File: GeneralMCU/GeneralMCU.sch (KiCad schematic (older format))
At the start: 98 parts, among them J1 ARM_JTAG_SWD, J2 SMD castellation PKG, J3 USB_B_Micro, J4 Conn_01x04, J5 PWR, J6 OLED, Q1 Q_NMOS_DGS, SW1 USER, SW2 RESET, U1 STM32F303R6Tx, U2 SN65HVD230, U3 AZ1117-3.3, U4 P78E05-1000, U5 DS18B20, Y1 32.768kHz, Y2 8MHz

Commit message: Can't remember these changes lol
From the meeting, switching back to branch now.
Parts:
- added snblock1, snblock2: Logo_Open_Hardware_Small, µ104KiCAD:SN_BLOCK, symbol Graphic:Logo_Open_Hardware_Small
- added snblock3, snblock4, snblock8: Logo_Open_Hardware_Small, µ104KiCAD:Paradigm_Logo_Very_Small, symbol Graphic:Logo_Open_Hardware_Small
- added snblock5: Logo_Open_Hardware_Small, Symbol:KiCad-Logo2_8mm_SilkScreen, symbol Graphic:Logo_Open_Hardware_Small
- added snblock6, snblock7: Logo_Open_Hardware_Small, Symbol:ESD-Logo_6.6x6mm_SilkScreen, symbol Graphic:Logo_Open_Hardware_Small
- F1: value 32VDC 1A PTC -> 3VDC 1A PTC
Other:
- note added: "*Vin = 9 - 30V\n\n"
- note removed: "*Vin = 9 - 32V\n\n"
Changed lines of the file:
@@
 $EndComp
 Text Notes 480  3290 0    39   ~ 0
-*Vin = 9 - 32V\n\n
+*Vin = 9 - 30V\n\n
 Wire Wire Line
 	1530 2970 1530 2890
@@
 P 1770 2970
 F 0 "F1" H 1690 3040 50  0000 C CNN
-F 1 "32VDC 1A PTC" H 1780 2910 28  0000 C CNN
+F 1 "3VDC 1A PTC" H 1780 2910 28  0000 C CNN
 F 2 "Diodes_SMD:D_1206" H 1770 2970 50  0001 C CNN
 F 3 "~" H 1770 2970 50  0001 C CNN
@@
 	1    0    0    -1
 $EndComp
+$Comp
+L Graphic:Logo_Open_Hardware_Small snblock1
+U 1 1 5DAB9BAE
+P 11960 7730
+F 0 "snblock1" H 11960 8005 50  0001 C CNN
+F 1 "Logo_Open_Hardware_Small" H 11960 7505 50  0001 C CNN
+F 2 "µ104KiCAD:SN_BLOCK" H 11960 7730 50  0001 C CNN
+F 3 "~" H 11960 7730 50  0001 C CNN
+	1    11960 7730
+	1    0    0    -1
+$EndComp
+$Comp
+L Graphic:Logo_Open_Hardware_Small snblock2
+U 1 1 5DABADF3
+P 11970 7300
+F 0 "snblock2" H 11970 7575 50  0001 C CNN
+F 1 "Logo_Open_Hardware_Small" H 11970 7075 50  0001 C CNN
+F 2 "µ104KiCAD:SN_BLOCK" H 11970 7300 50  0001 C CNN
+F 3 "~" H 11970 7300 50  0001 C CNN
+	1    11970 7300
+	1    0    0    -1
+$EndComp
+$Comp
+L Graphic:Logo_Open_Hardware_Small snblock3
+U 1 1 5DAEEBEF
+P 11960 6850
+F 0 "snblock3" H 11960 7125 50  0001 C CNN
+F 1 "Logo_Open_Hardware_Small" H 11960 6625 50  0001 C CNN
+F 2 "µ104KiCAD:Paradigm_Logo_Very_Small" H 11960 6850 50  0001 C CNN
+F 3 "~" H 11960 6850 50  0001 C CNN
+	1    11960 6850
+	1    0    0    -1
+$EndComp
+$Comp
+L Graphic:Logo_Open_Hardware_Small snblock4
+U 1 1 5DAF1C52
+P 11970 6400
+F 0 "snblock4" H 11970 6675 50  0001 C CNN
+F 1 "Logo_Open_Hardware_Small" H 11970 6175 50  0001 C CNN
+F 2 "µ104KiCAD:Paradigm_Logo_Very_Small" H 11970 6400 50  0001 C CNN
+F 3 "~" H 11970 6400 50  0001 C CNN
+	1    11970 6400
+	1    0    0    -1
+$EndComp
+$Comp
+L Graphic:Logo_Open_Hardware_Small snblock8
+U 1 1 5DAF1E56
+P 12500 6410
+F 0 "snblock8" H 12500 6685 50  0001 C CNN
+F 1 "Logo_Open_Hardware_Small" H 12500 6185 50  0001 C CNN
+F 2 "µ104KiCAD:Paradigm_Logo_Very_Small" H 12500 6410 50  0001 C CNN
+F 3 "~" H 12500 6410 50  0001 C CNN
+	1    12500 6410
+	1    0    0    -1
+$EndComp
+$Comp
+L Graphic:Logo_Open_Hardware_Small snblock6
+U 1 1 5DAF2182
+P 12480 6880
+F 0 "snblock6" H 12480 7155 50  0001 C CNN
+F 1 "Logo_Open_Hardware_Small" H 12480 6655 50  0001 C CNN
+F 2 "Symbol:ESD-Logo_6.6x6mm_SilkScreen" H 12480 6880 50  0001 C CNN
+F 3 "~" H 12480 6880 50  0001 C CNN
+	1    12480 6880
+	1    0    0    -1
+$EndComp
+$Comp
+L Graphic:Logo_Open_Hardware_Small snblock7
+U 1 1 5DAF2490
+P 12480 7310
+F 0 "snblock7" H 12480 7585 50  0001 C CNN
+F 1 "Logo_Open_Hardware_Small" H 12480 7085 50  0001 C CNN
+F 2 "Symbol:ESD-Logo_6.6x6mm_SilkScreen" H 12480 7310 50  0001 C CNN
+F 3 "~" H 12480 7310 50  0001 C CNN
+	1    12480 7310
+	1    0    0    -1
+$EndComp
+$Comp
+L Graphic:Logo_Open_Hardware_Small snblock5
+U 1 1 5DAF2789
+P 12470 7730
+F 0 "snblock5" H 12470 8005 50  0001 C CNN
+F 1 "Logo_Open_Hardware_Small" H 12470 7505 50  0001 C CNN
+F 2 "Symbol:KiCad-Logo2_8mm_SilkScreen" H 12470 7730 50  0001 C CNN
+F 3 "~" H 12470 7730 50  0001 C CNN
+	1    12470 7730
+	1    0    0    -1
+$EndComp

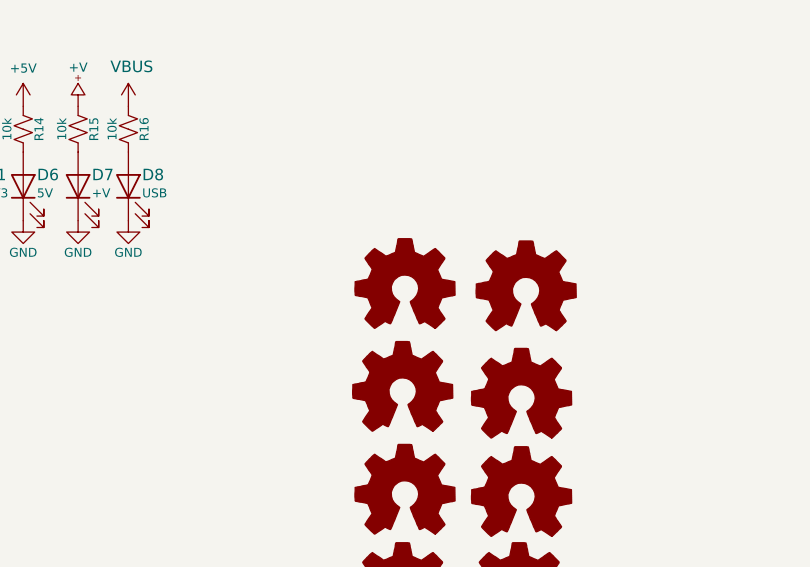
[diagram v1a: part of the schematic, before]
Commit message: Fixed castellated pads. Ready for review
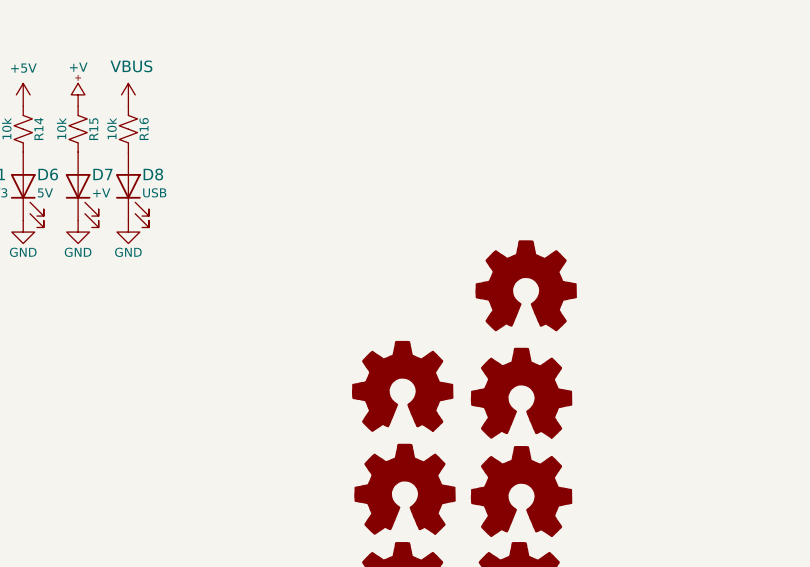
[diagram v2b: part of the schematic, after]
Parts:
- removed snblock4: Logo_Open_Hardware_Small, µ104KiCAD:Paradigm_Logo_Very_Small, symbol Graphic:Logo_Open_Hardware_Small
- snblock5: footprint Symbol:KiCad-Logo2_8mm_SilkScreen -> Symbol:KiCad-Logo_8mm_SilkScreen
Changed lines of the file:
@@
-$EndComp
-$Comp
-L Graphic:Logo_Open_Hardware_Small snblock4
-U 1 1 5DAF1C52
-P 11970 6400
-F 0 "snblock4" H 11970 6675 50  0001 C CNN
-F 1 "Logo_Open_Hardware_Small" H 11970 6175 50  0001 C CNN
-F 2 "µ104KiCAD:Paradigm_Logo_Very_Small" H 11970 6400 50  0001 C CNN
-F 3 "~" H 11970 6400 50  0001 C CNN
-	1    11970 6400
-	1    0    0    -1
 $EndComp
 $Comp
@@
 F 0 "snblock5" H 12470 8005 50  0001 C CNN
 F 1 "Logo_Open_Hardware_Small" H 12470 7505 50  0001 C CNN
-F 2 "Symbol:KiCad-Logo2_8mm_SilkScreen" H 12470 7730 50  0001 C CNN
+F 2 "Symbol:KiCad-Logo_8mm_SilkScreen" H 12470 7730 50  0001 C CNN
 F 3 "~" H 12470 7730 50  0001 C CNN
 	1    12470 7730

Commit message: Added silk and generated gerbers. Review me.
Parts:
- removed J2: SMD castellation PKG, µ104KiCAD:PAD42, symbol GeneralMCU-rescue:Conn_02x21_Counter_Clockwise-Connector_Generic
- added J2: SMD46 castellation PKG, µ104KiCAD:PAD42, symbol GeneralMCU-Example:SMD46
- added snblock10: Logo_Open_Hardware_Small, pics:stride, symbol Graphic:Logo_Open_Hardware_Small
- added snblock11: Logo_Open_Hardware_Small, pics:MUN, symbol Graphic:Logo_Open_Hardware_Small
- added snblock4: Logo_Open_Hardware_Small, pics:poddy, symbol Graphic:Logo_Open_Hardware_Small
- added snblock9: Logo_Open_Hardware_Small, pics:datboi, symbol Graphic:Logo_Open_Hardware_Small
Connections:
- net +3V3: now also J2.3
- net +5V: now also J2.2
- net +V: now also J2.26
- net CANH: now also J2.19
- net CANL: now also J2.18
- net CAN_Shield: now also J2.20
- net CHASSIS: now also J2.21
- net GND: now also J2.1, J2.22, J2.25
- net I2C1_SCL: now also J2.38
- net I2C1_SDA: now also J2.39
- net PA0: now also J2.44
- net PA1: now also J2.45
- net PA10: now also J2.27
- net PA2: now also J2.46
- net PA4: now also J2.4
- net PA5: now also J2.5
- net PA6: now also J2.6
- net PA7: now also J2.7
- net PA8: now also J2.29
- net PA9: now also J2.28
- net PB0: now also J2.10
- net PB1: now also J2.14
- net PB10: now also J2.12
- net PB11: now also J2.11
- net PB12: now also J2.15
- net PB13: now also J2.16
- net PB14: now also J2.17
- net PB15: now also J2.34
- net PB2: now also J2.13
- net PC0: now also J2.40
- net PC1: now also J2.41
- net PC10: now also J2.35
- net PC11: now also J2.36
- net PC12: now also J2.37
- net PC2: now also J2.42
- net PC3: now also J2.43
- net PC4: now also J2.8
- net PC5: now also J2.9
- net PC6: now also J2.33
- net PC7: now also J2.32
- net PC8: now also J2.31
- net PC9: now also J2.30
- no-connect marks 5 -> 7
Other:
- note added: "Drop In PCB Spec:\n1) CAN - Place TVS diode and bus filter caps close to CAN connector\n2) Provide power through J2 SMD pad within range from J5\n\n\n\nAssembly:\n1) Trim and file U4, and J6 THT flat on bottom off PCB\n2) Insert J3 jumper if powering over USB\n3) Solder jumper JP1 and JP2 for CAN terminations\n"
- note added: "GeneralMCU"
- note removed: "Drop In PCB Spec:\n1) CAN - Place TVS diode and bus filter caps close to CAN connector\n\n"
- note removed: "PARADUINO"

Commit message: Updated BOM
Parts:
- removed BZ1: Buzzer, Buzzer_Beeper:Buzzer_Murata_PKMCS0909E4000-R1, symbol GeneralMCU-rescue:Buzzer-Device
- removed C1, C11, C13, C15, C18, C19, C36, C6, C7, C9: 0.1u, µ104KiCAD_RLC:SMD_pkg_0603, symbol GeneralMCU-rescue:C_Small-Device
- removed C10, C12, C14, C16, C20, C34, C35: 1u, µ104KiCAD_RLC:SMD_pkg_0603, symbol GeneralMCU-rescue:C_Small-Device
- removed C17: DNP, µ104KiCAD_RLC:SMD_pkg_0603, symbol GeneralMCU-rescue:C_Small-Device
- removed C2, C3: 13p, µ104KiCAD_RLC:SMD_pkg_0603, symbol GeneralMCU-rescue:C_Small-Device
- removed C21: 4.7n, µ104KiCAD_RLC:SMD_pkg_0603, symbol GeneralMCU-rescue:C_Small-Device
- removed C22, C23: 0.1u, symbol GeneralMCU-rescue:C_Small-Device
- removed C24, C26: 1u, µ104KiCAD_RLC:SMD_pkg_1206, symbol GeneralMCU-rescue:C_Small-Device
- removed C25, C27, C33: 10u, µ104KiCAD_RLC:SMD_pkg_1206, symbol GeneralMCU-rescue:C_Small-Device
- removed C28: 22u, µ104KiCAD_RLC:SMD_pkg_1206, symbol GeneralMCU-rescue:C_Small-Device
- removed C4, C5: 8p, µ104KiCAD_RLC:SMD_pkg_0603, symbol GeneralMCU-rescue:C_Small-Device
- removed C8: 10n, µ104KiCAD_RLC:SMD_pkg_0603, symbol GeneralMCU-rescue:C_Small-Device
- removed D1: 3V3, LEDs:LED_0603, symbol GeneralMCU-rescue:LED-Device
- removed D2: WS2812B, LEDs:LED_WS2812-PLCC6, symbol GeneralMCU-rescue:WS2812-LED
- removed D3: NUP2105L, symbol GeneralMCU-rescue:D_TVS_x2_AAC-Device
- removed D4: D_TVS, Diodes_SMD:D_SMA, symbol GeneralMCU-rescue:D_TVS-Device
- removed D5: 40V 1A, Diodes_SMD:D_1206, symbol GeneralMCU-rescue:D_Schottky_Small_ALT-Device
- removed D6: 5V, LEDs:LED_0603, symbol GeneralMCU-rescue:LED-Device
- removed D7: +V, LEDs:LED_0603, symbol GeneralMCU-rescue:LED-Device
- removed D8: USB, LEDs:LED_0603, symbol GeneralMCU-rescue:LED-Device
- removed F1: 3VDC 1A PTC, Diodes_SMD:D_1206, symbol GeneralMCU-rescue:Fuse_Small-Device
- removed F2: 500mA PTC, Diodes_SMD:D_1206, symbol GeneralMCU-rescue:Fuse_Small-Device
- removed FB1, FB2: FB, µ104KiCAD_RLC:SMD_pkg_0805, symbol GeneralMCU-rescue:Ferrite_Bead_Small-Device
- removed H1, H2, H3, H4: M3, symbol GeneralMCU-rescue:MountingHole_Pad-Mechanical
- removed J1: ARM_JTAG_SWD, Connector_PinHeader_1.27mm:PinHeader_2x05_P1.27mm_Vertical_SMD, symbol GeneralMCU-rescue:Conn_ARM_JTAG_SWD_10-Connector
- removed J2: SMD46 castellation PKG, µ104KiCAD:PAD42, symbol GeneralMCU-Example:SMD46
- removed J3: USB_B_Micro, Connectors_USB:USB_Micro-B_Wuerth-629105150521_CircularHoles, symbol GeneralMCU-rescue:USB_B_Micro-Connector
- removed J4: Conn_01x04, symbol GeneralMCU-rescue:Conn_01x04-Connector_Generic
- removed J5: PWR, Pin_Headers:Pin_Header_Straight_1x02_Pitch2.54mm_SMD_Pin1Left, symbol GeneralMCU-rescue:Conn_01x02-Connector_Generic
- removed J6: OLED, µ104KiCAD:I2C_OLED, symbol GeneralMCU-rescue:Conn_01x04-Connector_Generic
- removed JP1, JP2, SB5, SB6: Jumper_NC_Small, µ104KiCAD:JUMPER_EGG, symbol GeneralMCU-rescue:Jumper_NC_Small-Device
- removed JP3: Jumper_NC_Small, Pin_Headers:Pin_Header_Straight_1x02_Pitch2.54mm_SMD_Pin1Left, symbol GeneralMCU-rescue:Jumper_NC_Small-Device
- removed Q1: Q_NMOS_DGS, Package_TO_SOT_SMD:SOT-23, symbol GeneralMCU-rescue:Q_NMOS_GSD-Device
- removed R1, R12, R13, R14, R15, R16, R2, R3: 10k, µ104KiCAD_RLC:SMD_pkg_0603, symbol GeneralMCU-rescue:R_Small_US-Device
- removed R10, R9: 1k, µ104KiCAD_RLC:SMD_pkg_0603, symbol GeneralMCU-rescue:R_Small_US-Device
- removed R11, R4, R6: 0, µ104KiCAD_RLC:SMD_pkg_0603, symbol GeneralMCU-rescue:R_Small_US-Device
- removed R18, R22, R23: 4.7k, µ104KiCAD_RLC:SMD_pkg_0603, symbol GeneralMCU-rescue:R_Small_US-Device
- removed R5: DNP, µ104KiCAD_RLC:SMD_pkg_0603, symbol GeneralMCU-rescue:R_Small_US-Device
- removed R7, R8: 60, µ104KiCAD_RLC:SMD_pkg_1210, symbol GeneralMCU-rescue:R_Small_US-Device
- removed SB1, SB2, SB3, SB4: Jumper_NC_Small, symbol GeneralMCU-rescue:Jumper_NC_Small-Device
- removed SW1: USER, Buttons_Switches_SMD:SW_SPST_B3U-1000P, symbol GeneralMCU-rescue:SW_Push-Switch
- removed SW2: RESET, Buttons_Switches_SMD:SW_SPST_B3U-1000P, symbol GeneralMCU-rescue:SW_Push-Switch
- removed TP1: 3V3, Measurement_Points:Measurement_Point_Round-SMD-Pad_Small, symbol GeneralMCU-rescue:TestPoint-Connector
- removed TP2: GND, Measurement_Points:Measurement_Point_Round-SMD-Pad_Small, symbol GeneralMCU-rescue:TestPoint-Connector
- removed TP3: 5V, Measurement_Points:Measurement_Point_Round-SMD-Pad_Small, symbol GeneralMCU-rescue:TestPoint-Connector
- removed TP5: +V, Measurement_Points:Measurement_Point_Round-SMD-Pad_Small, symbol GeneralMCU-rescue:TestPoint-Connector
- removed TP6: USB, Measurement_Points:Measurement_Point_Round-SMD-Pad_Small, symbol GeneralMCU-rescue:TestPoint-Connector
- removed U1: STM32F303R6Tx, Housings_QFP:LQFP-64_10x10mm_Pitch0.5mm, symbol GeneralMCU-rescue:STM32F303R6Tx-MCU_ST_STM32F3
- removed U2: SN65HVD230, µ104KiCAD_IC:SOIC-8_N, symbol GeneralMCU-rescue:SN65HVD230-Interface_CAN_LIN
- removed U3: AZ1117-3.3, TO_SOT_Packages_SMD:SOT-223-3_TabPin2, symbol GeneralMCU-rescue:AZ1117-3.3-Regulator_Linear
- removed U4: P78E05-1000, µ104KiCAD_DCDC:Recom_INNOLINE-R-78E, symbol GeneralMCU-rescue:V_REG-u104_KICAD_dcdc
- removed U5: DS18B20, µ104KiCAD_IC:MSOP-8, symbol GeneralMCU-rescue:DS18B20U-Sensor_Temperature
- removed Y1: 32.768kHz, µ104KiCAD_IC:Crystal_NDK_NX3215SA, symbol GeneralMCU-rescue:Crystal_Small-Device
- removed Y2: 8MHz, µ104KiCAD_IC:Crystal_L5_W3.2, symbol GeneralMCU-rescue:Crystal_Small-Device
- removed snblock1, snblock2: Logo_Open_Hardware_Small, µ104KiCAD:SN_BLOCK, symbol Graphic:Logo_Open_Hardware_Small
- removed snblock10: Logo_Open_Hardware_Small, pics:stride, symbol Graphic:Logo_Open_Hardware_Small
- removed snblock11: Logo_Open_Hardware_Small, pics:MUN, symbol Graphic:Logo_Open_Hardware_Small
- removed snblock3, snblock8: Logo_Open_Hardware_Small, µ104KiCAD:Paradigm_Logo_Very_Small, symbol Graphic:Logo_Open_Hardware_Small
- removed snblock4: Logo_Open_Hardware_Small, pics:poddy, symbol Graphic:Logo_Open_Hardware_Small
- removed snblock5: Logo_Open_Hardware_Small, Symbol:KiCad-Logo_8mm_SilkScreen, symbol Graphic:Logo_Open_Hardware_Small
- removed snblock6, snblock7: Logo_Open_Hardware_Small, Symbol:ESD-Logo_6.6x6mm_SilkScreen, symbol Graphic:Logo_Open_Hardware_Small
- removed snblock9: Logo_Open_Hardware_Small, pics:datboi, symbol Graphic:Logo_Open_Hardware_Small
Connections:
- no-connect marks 7 -> 0
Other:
- note removed: "*Place Close to Conn\n\n"
- note removed: "*Split termination improves the\nelectromagnetic emissions behavior of the network\nby eliminating fluctuations in the bus common mode voltages\nat the start and end of message transmissions\nLPF Cutoff f = 1/(2*pi*Rsplit*CSplit)\n= 564kHz\n\n"
- note removed: "*Under normal operation \npop. 1kΩ instead of C18\n\n"
- note removed: "*VDD Decoupling"
- note removed: "*VDDA Decoupling"
- note removed: "*Vin = 9 - 30V\n\n"
- note removed: "Assign Values and Spec\n"
- note removed: "CAN"
- note removed: "Drop In PCB Spec:\n1) CAN - Place TVS diode and bus filter caps close to CAN connector\n2) Provide power through J2 SMD pad within range from J5\n\n\n\nAssembly:\n1) Trim and file U4, and J6 THT flat on bottom off PCB\n2) Insert J3 jumper if powering over USB\n3) Solder jumper JP1 and JP2 for CAN terminations\n"
- note removed: "GeneralMCU"
- note removed: "MCU F303"
- note removed: "Mitchell Stride\nX\nX\n"
- note removed: "Peripherals\n"
- note removed: "Power\n\n"

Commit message: Used sch-bak to recover sch, updated pdf
-bak sch seemed to be correct so I just used that instead of a past commit.
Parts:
- added BZ1: Buzzer, Buzzer_Beeper:Buzzer_Murata_PKMCS0909E4000-R1, symbol GeneralMCU-rescue:Buzzer-Device
- added C1, C11, C13, C15, C18, C19, C36, C6, C7, C9: 0.1u, µ104KiCAD_RLC:SMD_pkg_0603, symbol GeneralMCU-rescue:C_Small-Device
- added C10, C12, C14, C16, C20, C34, C35: 1u, µ104KiCAD_RLC:SMD_pkg_0603, symbol GeneralMCU-rescue:C_Small-Device
- added C17: DNP, µ104KiCAD_RLC:SMD_pkg_0603, symbol GeneralMCU-rescue:C_Small-Device
- added C2, C3: 13p, µ104KiCAD_RLC:SMD_pkg_0603, symbol GeneralMCU-rescue:C_Small-Device
- added C21: 4.7n, µ104KiCAD_RLC:SMD_pkg_0603, symbol GeneralMCU-rescue:C_Small-Device
- added C22, C23: 0.1u, symbol GeneralMCU-rescue:C_Small-Device
- added C24, C26: 1u, µ104KiCAD_RLC:SMD_pkg_1206, symbol GeneralMCU-rescue:C_Small-Device
- added C25, C27, C33: 10u, µ104KiCAD_RLC:SMD_pkg_1206, symbol GeneralMCU-rescue:C_Small-Device
- added C28: 22u, µ104KiCAD_RLC:SMD_pkg_1206, symbol GeneralMCU-rescue:C_Small-Device
- added C4, C5: 8p, µ104KiCAD_RLC:SMD_pkg_0603, symbol GeneralMCU-rescue:C_Small-Device
- added C8: 10n, µ104KiCAD_RLC:SMD_pkg_0603, symbol GeneralMCU-rescue:C_Small-Device
- added D1: 3V3, LEDs:LED_0603, symbol GeneralMCU-rescue:LED-Device
- added D2: WS2812B, LEDs:LED_WS2812-PLCC6, symbol GeneralMCU-rescue:WS2812-LED
- added D3: NUP2105L, symbol GeneralMCU-rescue:D_TVS_x2_AAC-Device
- added D4: D_TVS, Diodes_SMD:D_SMA, symbol GeneralMCU-rescue:D_TVS-Device
- added D5: 40V 1A, Diodes_SMD:D_1206, symbol GeneralMCU-rescue:D_Schottky_Small_ALT-Device
- added D6: 5V, LEDs:LED_0603, symbol GeneralMCU-rescue:LED-Device
- added D7: +V, LEDs:LED_0603, symbol GeneralMCU-rescue:LED-Device
- added D8: USB, LEDs:LED_0603, symbol GeneralMCU-rescue:LED-Device
- added F1: PTC, Diodes_SMD:D_1206, symbol GeneralMCU-rescue:Fuse_Small-Device
- added F2: 500mA PTC, Diodes_SMD:D_1206, symbol GeneralMCU-rescue:Fuse_Small-Device
- added FB1, FB2: FB, µ104KiCAD_RLC:SMD_pkg_0805, symbol GeneralMCU-rescue:Ferrite_Bead_Small-Device
- added H1, H2, H3, H4: M3, symbol GeneralMCU-rescue:MountingHole_Pad-Mechanical
- added J1: ARM_JTAG_SWD, Connector_PinHeader_1.27mm:PinHeader_2x05_P1.27mm_Vertical_SMD, symbol GeneralMCU-rescue:Conn_ARM_JTAG_SWD_10-Connector
- added J2: SMD46 castellation PKG, µ104KiCAD:PAD42, symbol GeneralMCU-Example:SMD46
- added J3: USB_B_Micro, Connectors_USB:USB_Micro-B_Wuerth-629105150521_CircularHoles, symbol GeneralMCU-rescue:USB_B_Micro-Connector
- added J4: Conn_01x04, symbol GeneralMCU-rescue:Conn_01x04-Connector_Generic
- added J5: PWR, Pin_Headers:Pin_Header_Straight_1x02_Pitch2.54mm_SMD_Pin1Left, symbol GeneralMCU-rescue:Conn_01x02-Connector_Generic
- added J6: OLED, µ104KiCAD:I2C_OLED, symbol GeneralMCU-rescue:Conn_01x04-Connector_Generic
- added JP1, JP2, SB5, SB6: Jumper_NC_Small, µ104KiCAD:JUMPER_EGG, symbol GeneralMCU-rescue:Jumper_NC_Small-Device
- added JP3: Jumper_NC_Small, Pin_Headers:Pin_Header_Straight_1x02_Pitch2.54mm_SMD_Pin1Left, symbol GeneralMCU-rescue:Jumper_NC_Small-Device
- added R1, R12, R13, R14, R15, R16, R2, R3: 10k, µ104KiCAD_RLC:SMD_pkg_0603, symbol GeneralMCU-rescue:R_Small_US-Device
- added R10, R9: 1k, µ104KiCAD_RLC:SMD_pkg_0603, symbol GeneralMCU-rescue:R_Small_US-Device
- added R11, R4, R6: 0, µ104KiCAD_RLC:SMD_pkg_0603, symbol GeneralMCU-rescue:R_Small_US-Device
- added R18, R22, R23: 4.7k, µ104KiCAD_RLC:SMD_pkg_0603, symbol GeneralMCU-rescue:R_Small_US-Device
- added R5: DNP, µ104KiCAD_RLC:SMD_pkg_0603, symbol GeneralMCU-rescue:R_Small_US-Device
- added R7, R8: 60, µ104KiCAD_RLC:SMD_pkg_1210, symbol GeneralMCU-rescue:R_Small_US-Device
- added SB1, SB2, SB3, SB4: Jumper_NC_Small, symbol GeneralMCU-rescue:Jumper_NC_Small-Device
- added SW1: USER, Buttons_Switches_SMD:SW_SPST_B3U-1000P, symbol GeneralMCU-rescue:SW_Push-Switch
- added SW2: RESET, Buttons_Switches_SMD:SW_SPST_B3U-1000P, symbol GeneralMCU-rescue:SW_Push-Switch
- added TP1: 3V3, Measurement_Points:Measurement_Point_Round-SMD-Pad_Small, symbol GeneralMCU-rescue:TestPoint-Connector
- added TP2: GND, Measurement_Points:Measurement_Point_Round-SMD-Pad_Small, symbol GeneralMCU-rescue:TestPoint-Connector
- added TP3: 5V, Measurement_Points:Measurement_Point_Round-SMD-Pad_Small, symbol GeneralMCU-rescue:TestPoint-Connector
- added TP5: +V, Measurement_Points:Measurement_Point_Round-SMD-Pad_Small, symbol GeneralMCU-rescue:TestPoint-Connector
- added TP6: USB, Measurement_Points:Measurement_Point_Round-SMD-Pad_Small, symbol GeneralMCU-rescue:TestPoint-Connector
- added U1: STM32F303R6Tx, Housings_QFP:LQFP-64_10x10mm_Pitch0.5mm, symbol GeneralMCU-rescue:STM32F303R6Tx-MCU_ST_STM32F3
- added U2: SN65HVD230, µ104KiCAD_IC:SOIC-8_N, symbol GeneralMCU-rescue:SN65HVD230-Interface_CAN_LIN
- added U3: AZ1117-3.3, TO_SOT_Packages_SMD:SOT-223-3_TabPin2, symbol GeneralMCU-rescue:AZ1117-3.3-Regulator_Linear
- added U4: P78E05-1000, µ104KiCAD_DCDC:Recom_INNOLINE-R-78E, symbol GeneralMCU-rescue:V_REG-u104_KICAD_dcdc
- added U5: DS18B20, µ104KiCAD_IC:MSOP-8, symbol GeneralMCU-rescue:DS18B20U-Sensor_Temperature
- added Y1: 32.768kHz, µ104KiCAD_IC:Crystal_NDK_NX3215SA, symbol GeneralMCU-rescue:Crystal_Small-Device
- added Y2: 8MHz, µ104KiCAD_IC:Crystal_L5_W3.2, symbol GeneralMCU-rescue:Crystal_Small-Device
- added e: Q_NMOS_DGS, Package_TO_SOT_SMD:SOT-23, symbol GeneralMCU-rescue:Q_NMOS_GSD-Device
- added snblock1, snblock2: Logo_Open_Hardware_Small, µ104KiCAD:SN_BLOCK, symbol Graphic:Logo_Open_Hardware_Small
- added snblock10: Logo_Open_Hardware_Small, pics:stride, symbol Graphic:Logo_Open_Hardware_Small
- added snblock11: Logo_Open_Hardware_Small, pics:MUN, symbol Graphic:Logo_Open_Hardware_Small
- added snblock3, snblock8: Logo_Open_Hardware_Small, µ104KiCAD:Paradigm_Logo_Very_Small, symbol Graphic:Logo_Open_Hardware_Small
- added snblock4: Logo_Open_Hardware_Small, pics:poddy, symbol Graphic:Logo_Open_Hardware_Small
- added snblock5: Logo_Open_Hardware_Small, Symbol:KiCad-Logo_8mm_SilkScreen, symbol Graphic:Logo_Open_Hardware_Small
- added snblock6, snblock7: Logo_Open_Hardware_Small, Symbol:ESD-Logo_6.6x6mm_SilkScreen, symbol Graphic:Logo_Open_Hardware_Small
- added snblock9: Logo_Open_Hardware_Small, pics:datboi, symbol Graphic:Logo_Open_Hardware_Small
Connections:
- new net: C35.1, D2.3 (VCC), R12.1
- new net: H1.1, SB1.2
- new net: H2.1, SB2.2
- new net: H3.1, SB3.2
- new net: H4.1, SB4.2
- new net: BZ1.1 (-), R11.1
- new net: BZ1.2 (+), e.3 (D)
- new net: F2.1, J3.1 (VBUS)
- new net: R10.1, R9.2, e.1 (G)
- new net: C17.2, R4.2, U2.1 (D)
- new net: R6.2, U2.4 (R)
- new net: C18.2, R5.1, U2.8 (Rs)
- new net: JP1.1, R7.1
- new net: JP2.1, R8.2
- new net: D5.2 (A), F1.2
- new net: C25.1, D5.1 (K), FB1.2
- new net: C27.1, FB1.1, U4.1 (VI)
- new net: F2.2, FB2.2
- new net: D1.2 (A), R13.1
- new net: D6.2 (A), R14.1
- new net: D8.2 (A), R16.1
- new net: D7.2 (A), R15.1
- new net +3V3: C10.1, C11.1, C12.1, C13.1, C14.1, C15.1, C16.1, C19.1, C20.1, C26.1, C36.2, C7.1, C8.1, C9.1, J1.1 (VCC), J2.3, J6.1 (Pin_1), R1.2, R13.2, R18.2, R2.2, R22.2, R23.2, TP1.1, U1.1 (VBAT), U1.13 (VDDA), U1.19 (VDD), U1.32 (VDD), U1.48 (VDD), U1.64 (VDD), U2.3 (VCC), U3.2 (VO), U5.8 (VDD)
- new net +5V: C24.1, C28.1, D2.5 (VDD), J2.2, JP3.2, R11.2, R12.2, R14.2, TP3.1, U3.3 (VI), U4.3 (VO)
- new net +V: D4.1 (A1), F1.1, J2.26, J5.2 (Pin_2), R15.2, TP5.1
- new net BOOT0: R3.2, U1.60 (BOOT0)
- new net BUZZ: R9.1, U1.57 (PB5)
- new net CANH: C22.1, D3.1 (A1), J2.19, J4.4 (Pin_4), JP1.2, U2.7 (CANH)
- new net CANL: C23.1, D3.2 (A2), J2.18, J4.3 (Pin_3), JP2.2, U2.6 (CANL)
- new net CAN_RX: R6.1, U1.61 (PB8)
- new net CAN_Shield: J2.20, J4.2 (Pin_2), SB5.1
- new net CAN_TX: R4.1, U1.62 (PB9)
- new net CHASSIS: D4.2 (A2), J2.21, SB1.1, SB2.1, SB3.1, SB4.1, SB6.2
- new net GND: C1.2, C10.2, C11.2, C12.2, C13.2, C14.2, C15.2, C16.2, C17.1, C18.1, C19.2, C2.2, C20.2, C21.1, C22.2, C23.2, C24.2, C25.2, C26.2, C27.2, C28.2, C3.2, C33.2, C34.2, C35.2, C36.1, C4.2, C5.2, C6.2, C7.2, C8.2, C9.2, D1.1 (K), D2.6 (VSS), D3.3 (common), D6.1 (K), D7.1 (K), D8.1 (K), J1.3 (GND), J1.5 (GND), J1.9 (GNDDetect), J2.1, J2.22, J2.25, J3.5 (GND), J3.6 (Shield), J4.1 (Pin_1), J5.1 (Pin_1), J6.2 (Pin_2), R10.2, R3.1, SB5.2, SB6.1, SW1.1, SW2.1, TP2.1, U1.12 (VSSA), U1.18 (VSS), U1.31 (VSS), U1.47 (VSS), U1.63 (VSS), U2.2 (GND), U3.1 (GND), U4.2 (GND), U5.4 (GND), e.2 (S)
- new net I2C1_SCL: J2.38, J6.3 (Pin_3), R23.1, U1.58 (PB6)
- new net I2C1_SDA: J2.39, J6.4 (Pin_4), R22.1, U1.59 (PB7)
- new net JTAG_JTDI: J1.8 (NC/TDI), U1.50 (PA15)
- new net JTAG_JTDO: J1.6 (SWO/TDO), U1.55 (PB3)
- new net JTAG_NJTRST: J1.10 (~RESET~), U1.56 (PB4)
- new net JTAG_SWDCLK\TCK: J1.4 (SWDCLK/TCK), U1.49 (PA14)
- new net JTAG_SWDIO\TMS: J1.2 (SWDIO/TMS), U1.46 (PA13)
- new net NRST: C6.1, R2.1, SW2.2, U1.7 (NRST)
- new net OSC32_IN: C2.1, U1.3 (PC14), Y1.1
- new net OSC32_OUT: C3.1, U1.4 (PC15), Y1.2
- new net OSC_IN: C4.1, U1.5 (PF0), Y2.1
- new net OSC_OUT: C5.1, U1.6 (PF1), Y2.2
- new net PA0: J2.44, U1.14 (PA0)
- new net PA1: J2.45, U1.15 (PA1)
- new net PA10: J2.27, U1.43 (PA10)
- new net PA2: J2.46, U1.16 (PA2)
- new net PA4: J2.4, U1.20 (PA4)
- new net PA5: J2.5, U1.21 (PA5)
- new net PA6: J2.6, U1.22 (PA6)
- new net PA7: J2.7, U1.23 (PA7)
- new net PA8: J2.29, U1.41 (PA8)
- new net PA9: J2.28, U1.42 (PA9)
- new net PB0: J2.10, U1.26 (PB0)
- new net PB1: J2.14, U1.27 (PB1)
- new net PB10: J2.12, U1.29 (PB10)
- new net PB11: J2.11, U1.30 (PB11)
- new net PB12: J2.15, U1.33 (PB12)
- new net PB13: J2.16, U1.34 (PB13)
- new net PB14: J2.17, U1.35 (PB14)
- new net PB15: J2.34, U1.36 (PB15)
- new net PB2: J2.13, U1.28 (PB2)
- new net PC0: J2.40, U1.8 (PC0)
- new net PC1: J2.41, U1.9 (PC1)
- new net PC10: J2.35, U1.51 (PC10)
- new net PC11: J2.36, U1.52 (PC11)
- new net PC12: J2.37, U1.53 (PC12)
- new net PC13: C1.1, R1.1, SW1.2, U1.2 (PC13)
- new net PC2: J2.42, U1.10 (PC2)
- new net PC3: J2.43, U1.11 (PC3)
- new net PC4: J2.8, U1.24 (PC4)
- new net PC5: J2.9, U1.25 (PC5)
- new net PC6: J2.33, U1.37 (PC6)
- new net PC7: J2.32, U1.38 (PC7)
- new net PC8: J2.31, U1.39 (PC8)
- new net PC9: J2.30, U1.40 (PC9)
- new net PD2: R18.1, U1.54 (PD2), U5.1 (DQ)
- new net Rs: R5.2
- new net USB_DM: J3.2 (D-), U1.44 (PA11)
- new net USB_DP: J3.3 (D+), U1.45 (PA12)
- new net USR_LED: D2.2 (DIN), U1.17 (PA3)
- new net VBUS: C33.1, C34.1, FB2.1, JP3.1, R16.2, TP6.1
- new net Vref: C21.2, R7.2, R8.1, U2.5 (Vref)
- no-connect marks 0 -> 7
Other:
- note added: "*Place Close to Conn\n\n"
- note added: "*Split termination improves the\nelectromagnetic emissions behavior of the network\nby eliminating fluctuations in the bus common mode voltages\nat the start and end of message transmissions\nLPF Cutoff f = 1/(2*pi*Rsplit*CSplit)\n= 564kHz\n\n"
- note added: "*Under normal operation \npop. 1kΩ instead of C18\n\n"
- note added: "*VDD Decoupling"
- note added: "*VDDA Decoupling"
- note added: "*Vin = 9 - 30V\n\n"
- note added: "Assign Values and Spec\n"
- note added: "CAN"
- note added: "Drop In PCB Spec:\n1) CAN - Place TVS diode and bus filter caps close to CAN connector\n2) Provide power through J2 SMD pad within range from J5\n\n\n\nAssembly:\n1) Trim and file U4, and J6 THT flat on bottom off PCB\n2) Insert J3 jumper if powering over USB\n3) Solder jumper JP1 and JP2 for CAN terminations\n"
- note added: "GeneralMCU"
- note added: "MCU F303"
- note added: "Mitchell Stride\nX\nX\n"
- note added: "Peripherals\n"
- note added: "Power\n\n"
